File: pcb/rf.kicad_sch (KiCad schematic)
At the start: 34 parts, among them J10 73412-0114, J12 73412-0114, U4 MAX-M10S, Y3 ECS-TXO-25CSMV-320-AM-TR

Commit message: reroute done! except for the gps which I'm currently verifying my implementation on
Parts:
- removed C40, C55: 100nF, Capacitor_SMD:C_0402_1005Metric, symbol Device:C
- removed C50, C51: C, Capacitor_SMD:C_0402_1005Metric, symbol Device:C
- removed L9: L, Inductor_SMD:L_0402_1005Metric, symbol Device:L
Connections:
- net +3.3V: no longer U4.14 (VCC_RF), U4.6 (V_BCKP)
- net at U4.11 (RF_IN): now also J12.1 (SIGNAL)
- no-connect marks 17 -> 19

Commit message: added models for some things, fixed micro sd impl and a bunch of other stuff - pcb currently probably ready for production
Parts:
- renumbered C25 to C18, C26 to C19, C27 to C20, C28 to C21, C29 to C22, C30 to C23, C31 to C24, C32 to C25, C33 to C26, C34 to C27, C35 to C28, C36 to C29, C37 to C30, C38 to C31, C54 to C32, C53 to C33, C39 to C34, J10 to J7, J12 to J8, L2 to L1, L3 to L2, L4 to L3, L5 to L4, L6 to L5, L7 to L6, L8 to L7, U4 to U3, Y3 to Y1

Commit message: mainly worked on bom (still just on google sheets), but while doing so fixed some issues and redid some component selection
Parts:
- removed J7, J8: 73412-0114, footprints:73412-0110, symbol 73412-0114:73412-0114
- added J3, J5: Conn_Coaxial, Connector_Coaxial:U.FL_Hirose_U.FL-R-SMT-1_Vertical, symbol Connector:Conn_Coaxial
- L7: footprint Inductor_SMD:L_0805_2012Metric -> Inductor_SMD:L_0603_1608Metric
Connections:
- net GND: now also J3.2 (Ext), J5.2 (Ext)
- net at C22.2, C26.2, L2.2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: now also J5.1 (In)
- net at U3.11 (RF_IN): now also J3.1 (In)

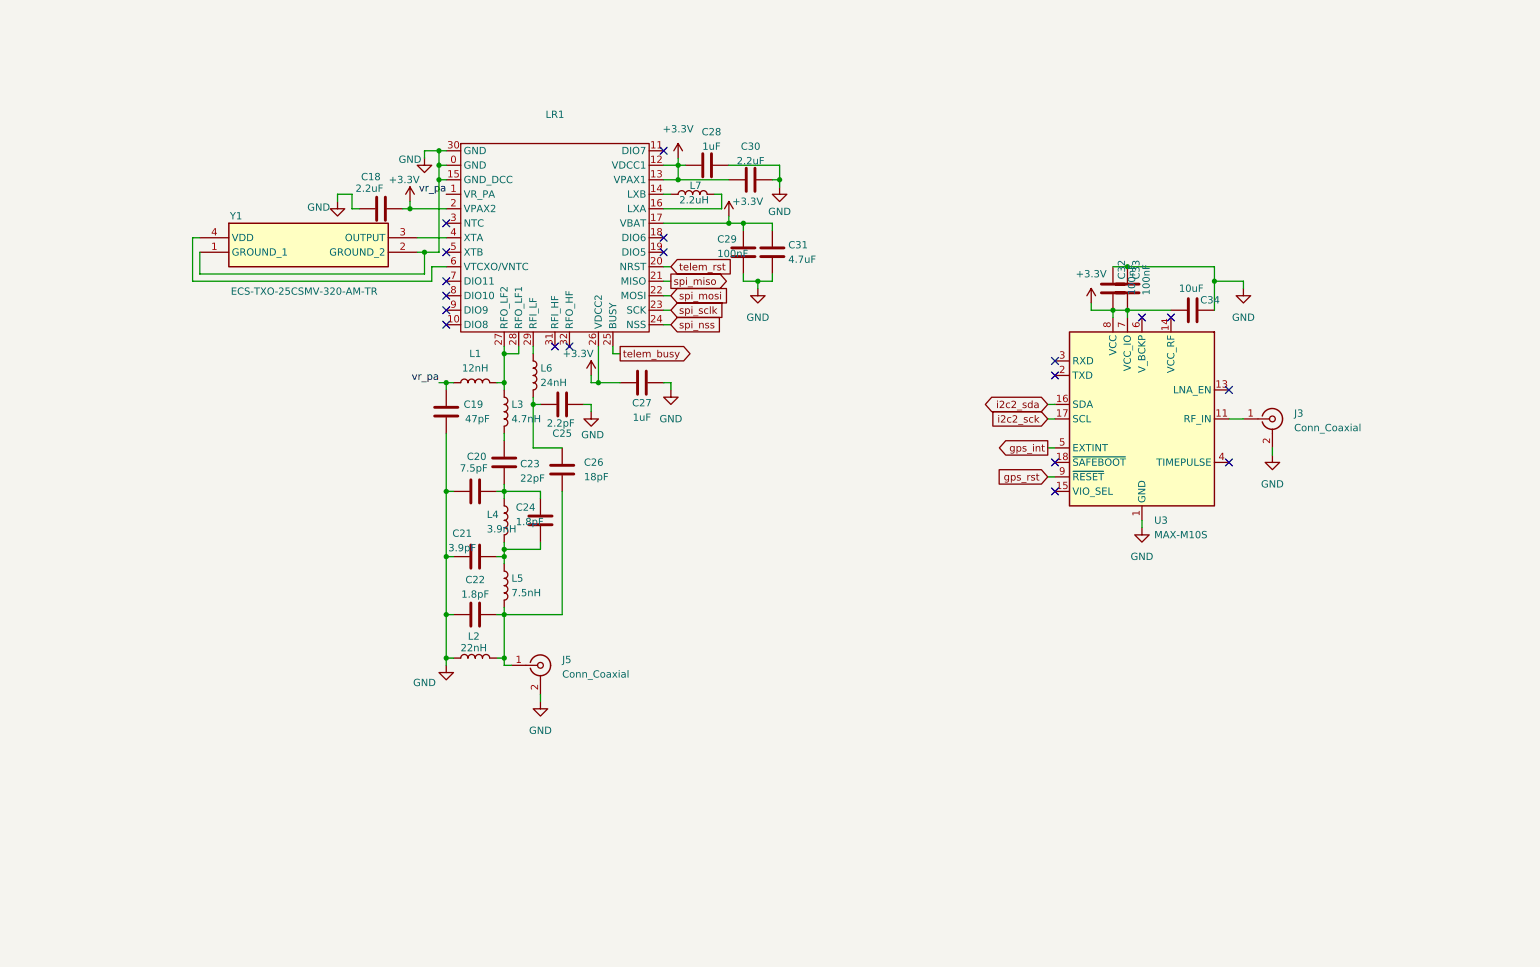
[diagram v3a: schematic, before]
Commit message: reorganized schematic, started to add a readme (not really though), also pcb updated
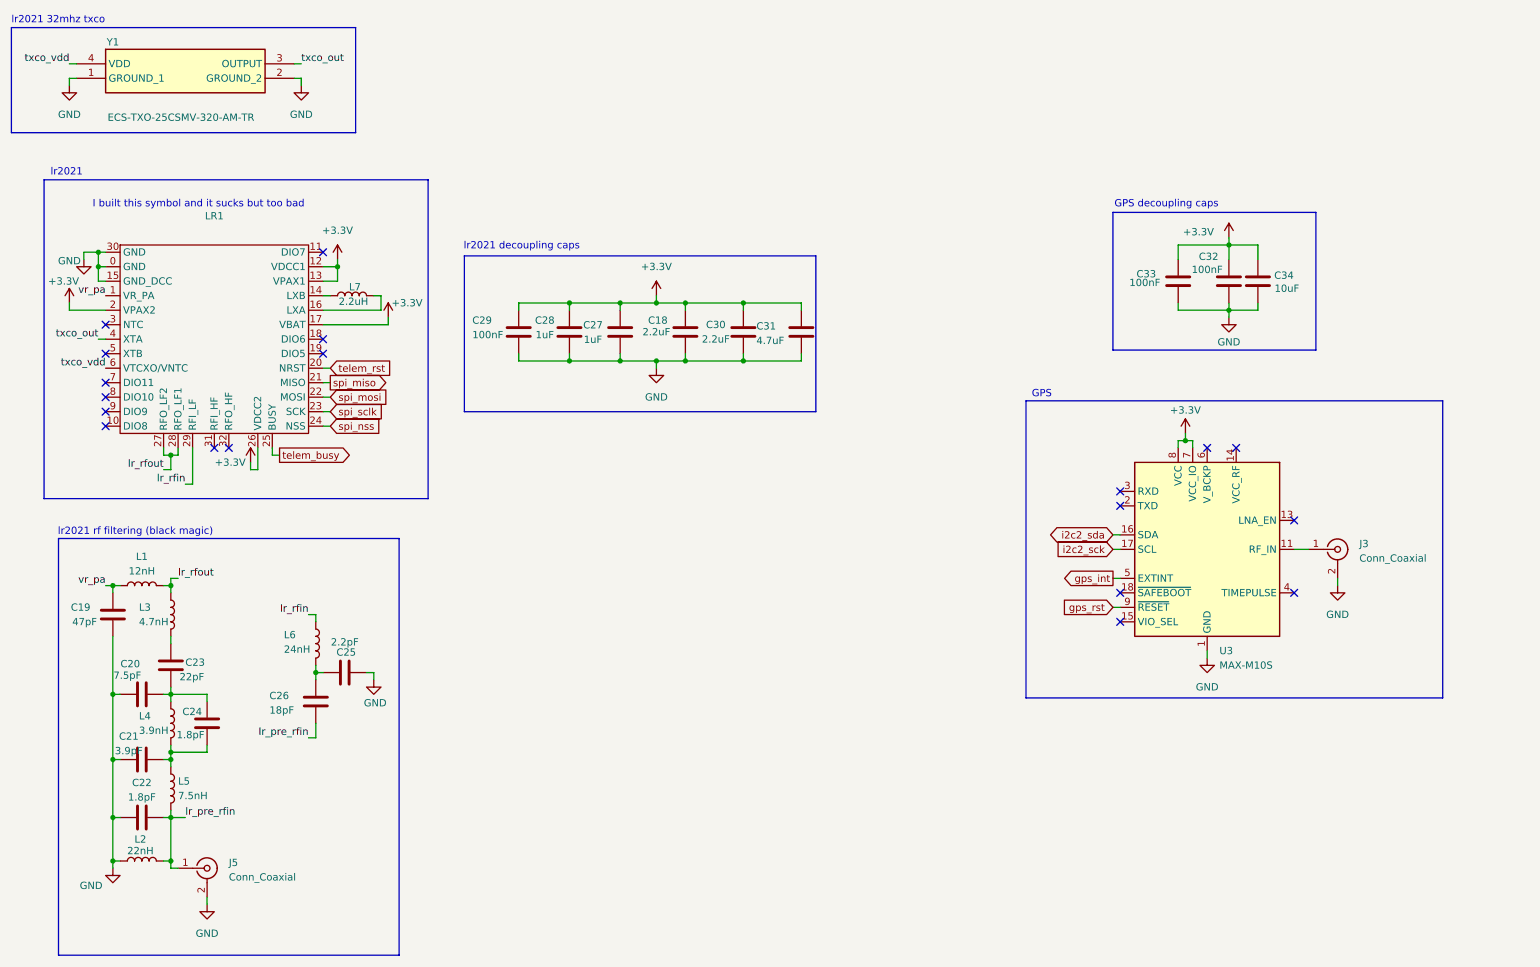
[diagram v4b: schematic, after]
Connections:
- net +3.3V: now also C28.2, C30.2, C32.2; no longer C28.1, C30.1, C32.1
- net GND: now also C28.1, C30.1, C32.1; no longer C28.2, C30.2, C32.2
- net lr_pre_rfin: now reaches C22.2, C26.2, J5.1 (In), L2.2, L5.2
- net lr_rfout: now reaches L1.2, L3.1, LR1.27 (RFO_LF2), LR1.28 (RFO_LF1)
- net txco_out: now reaches LR1.4 (XTA), Y1.3 (OUTPUT)
- net txco_vdd: now reaches LR1.6 (VTCXO/VNTC), Y1.4 (VDD)
- net lr_rfin: now reaches L6.1, LR1.29 (RFI_LF)
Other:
- note added: "GPS"
- note added: "GPS decoupling caps"
- note added: "I built this symbol and it sucks but too bad"
- note added: "lr2021"
- note added: "lr2021 32mhz txco"
- note added: "lr2021 decoupling caps"
- note added: "lr2021 rf filtering (black magic)"
- moved on the sheet: C18, C19, C20, C21, C22, C23, C24, C25, C26, C27, C28, C29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

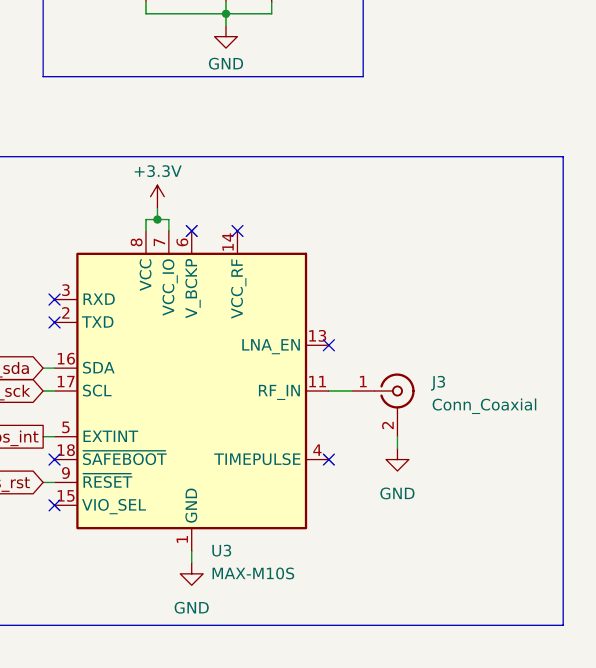
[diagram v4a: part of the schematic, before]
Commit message: modified gps for an active antenna
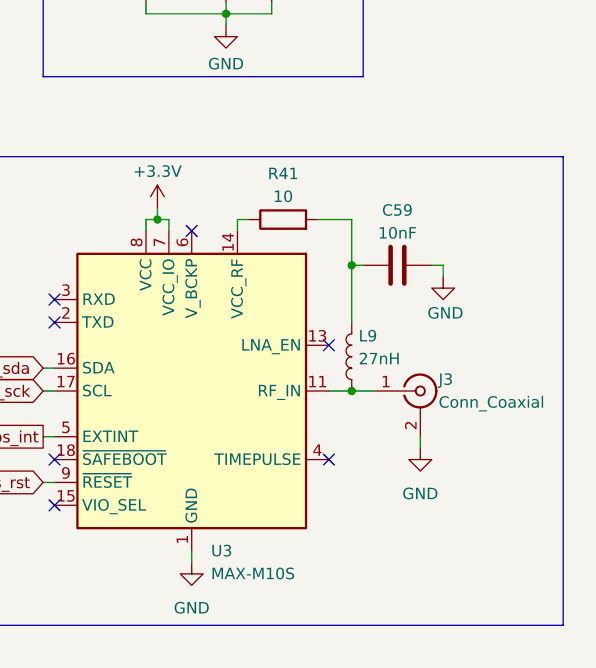
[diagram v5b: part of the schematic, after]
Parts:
- added C59: 10nF, Capacitor_SMD:C_0402_1005Metric, symbol Device:C
- added L9: 27nH, Inductor_SMD:L_0402_1005Metric, symbol Device:L
- added R41: 10, Resistor_SMD:R_0603_1608Metric, symbol Device:R
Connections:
- net GND: now also C59.2
- net at J3.1 (In), U3.11 (RF_IN): now also L9.1
- net at U3.14 (VCC_RF): now also R41.1
- new net: C59.1, L9.2, R41.2
- no-connect marks 19 -> 18
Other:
- moved on the sheet: J3
